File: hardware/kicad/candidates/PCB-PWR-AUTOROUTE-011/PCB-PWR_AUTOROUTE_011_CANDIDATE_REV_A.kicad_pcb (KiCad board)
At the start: 4 copper layers, 90 x 60 mm, 66 parts, among them J1 43045-0213, J2 43045-1202, Q1 CSD18540Q5B, U1 LM74700QDBVRQ1, U2 INA226AIDGSR, U3 LMR604403SRAKR, U4 LMR604403SRAKR, U5 TPS7A2018PDBVR

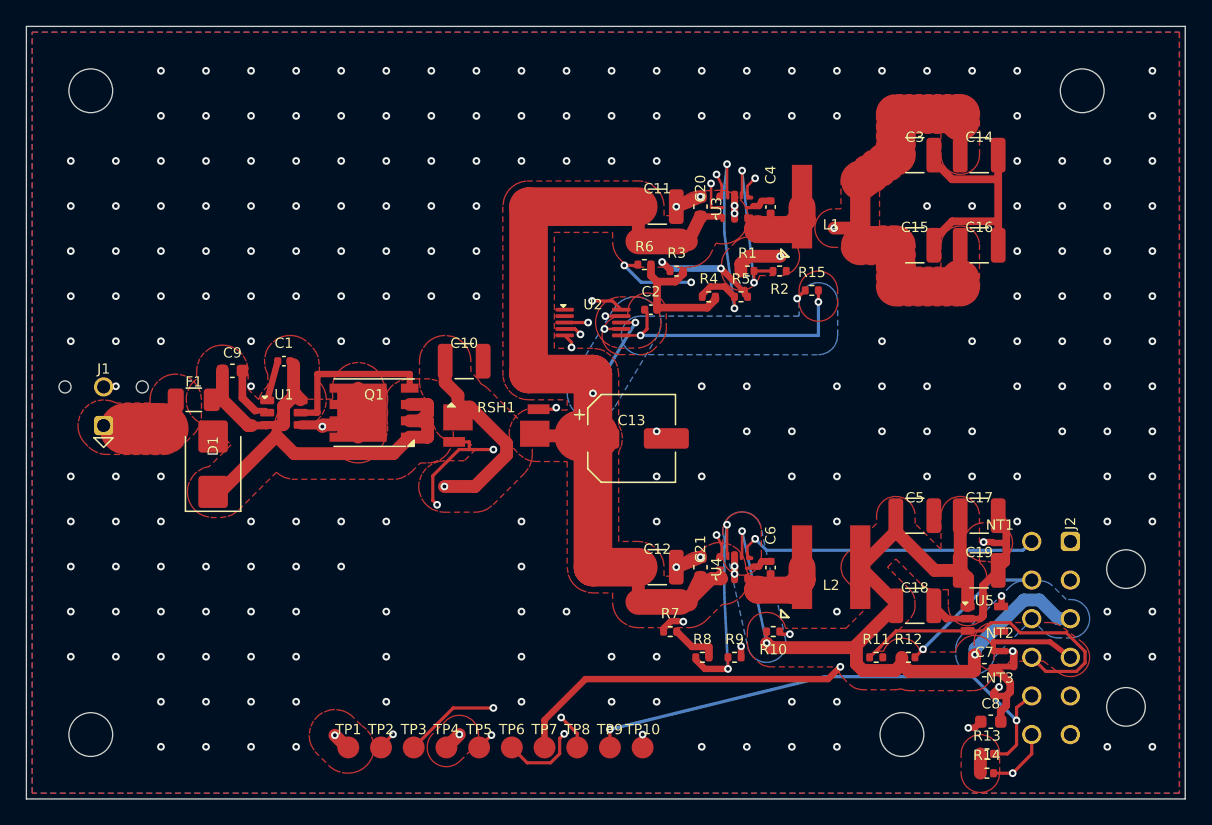
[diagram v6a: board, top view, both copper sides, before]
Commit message: apply: tools/apply_pcb_pwr_autoroute_candidate_rev_a.py
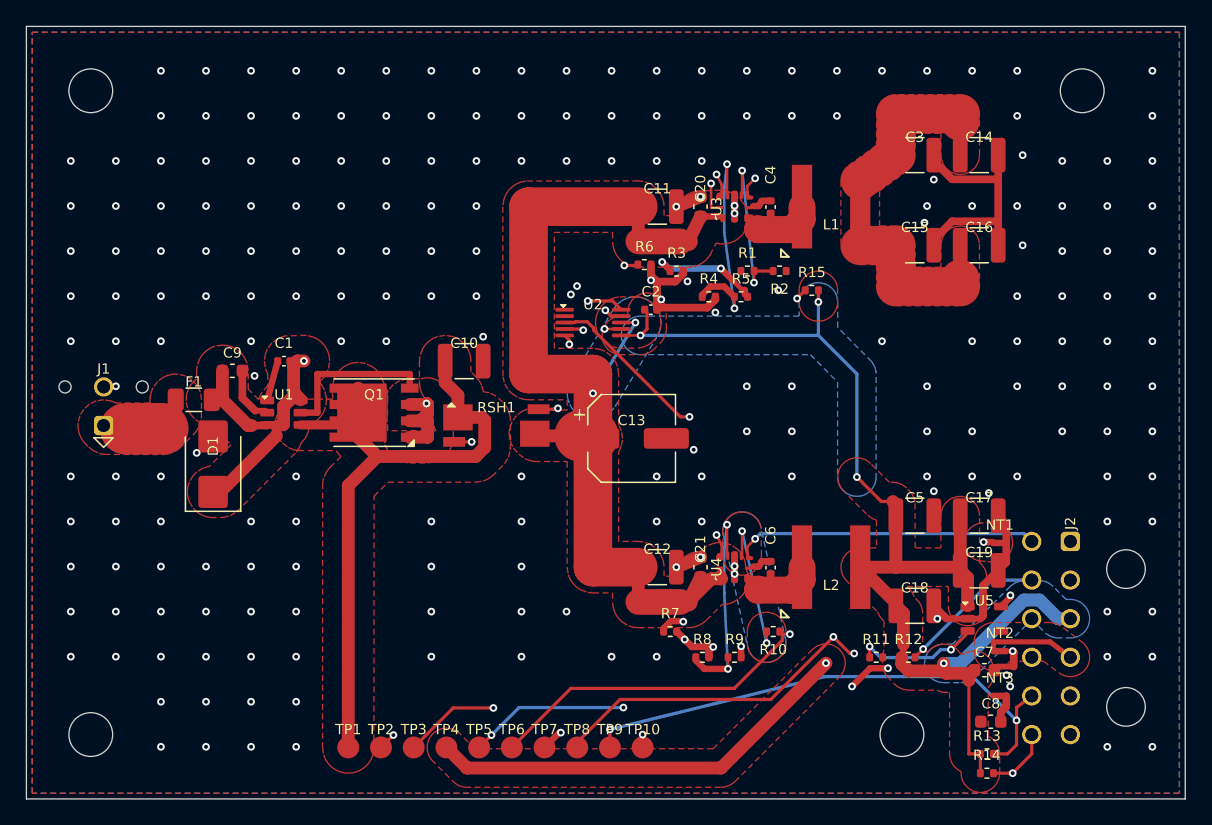
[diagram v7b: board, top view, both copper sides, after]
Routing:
- net 3V8_MODEM: track 144.0 -> 91.7 mm, vias 3 -> 1
- net 1V8_MIC: track 70.4 -> 52.3 mm, vias 3 -> 4
- net 3V3_DIGITAL: track 91.4 -> 106.1 mm, vias 5 -> 6
- net EN_MODEM: track 57.1 -> 67.7 mm, vias 3 -> 2
- net SHUNT_LOAD_SENSE: track 45.3 -> 55.1 mm
- net EN_AUX: track 24.5 -> 16.4 mm, vias 0 -> 2
- net GND_MIC: track 7.95 -> 0.00 mm, vias 1 -> 0
- net VBAT_PROTECTED: track 60.1 -> 52.6 mm, vias 3 -> 0
- net PWR_GOOD: track 65.0 -> 58.0 mm, vias 3 -> 2
- net I2C2_SDA: track 83.1 -> 77.7 mm
- net PG_3V8: track 67.0 -> 63.3 mm, vias 3 -> 4
- net I2C2_SCL: track 78.2 -> 75.0 mm
- net GND_PWR: track 65.5 -> 62.7 mm, vias 220 -> 224
- net SHUNT_SOURCE_SENSE: track 47.8 -> 45.6 mm, vias 4 -> 3
- net FAULT: track 77.0 -> 77.6 mm, vias 3 -> 4
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- added copper zone on In2.Cu, net VBAT_FUSED
- removed copper zone on In2.Cu, net VBAT_PROTECTED

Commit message: apply: tools/apply_pcb_pwr_autoroute_candidate_rev_a.py
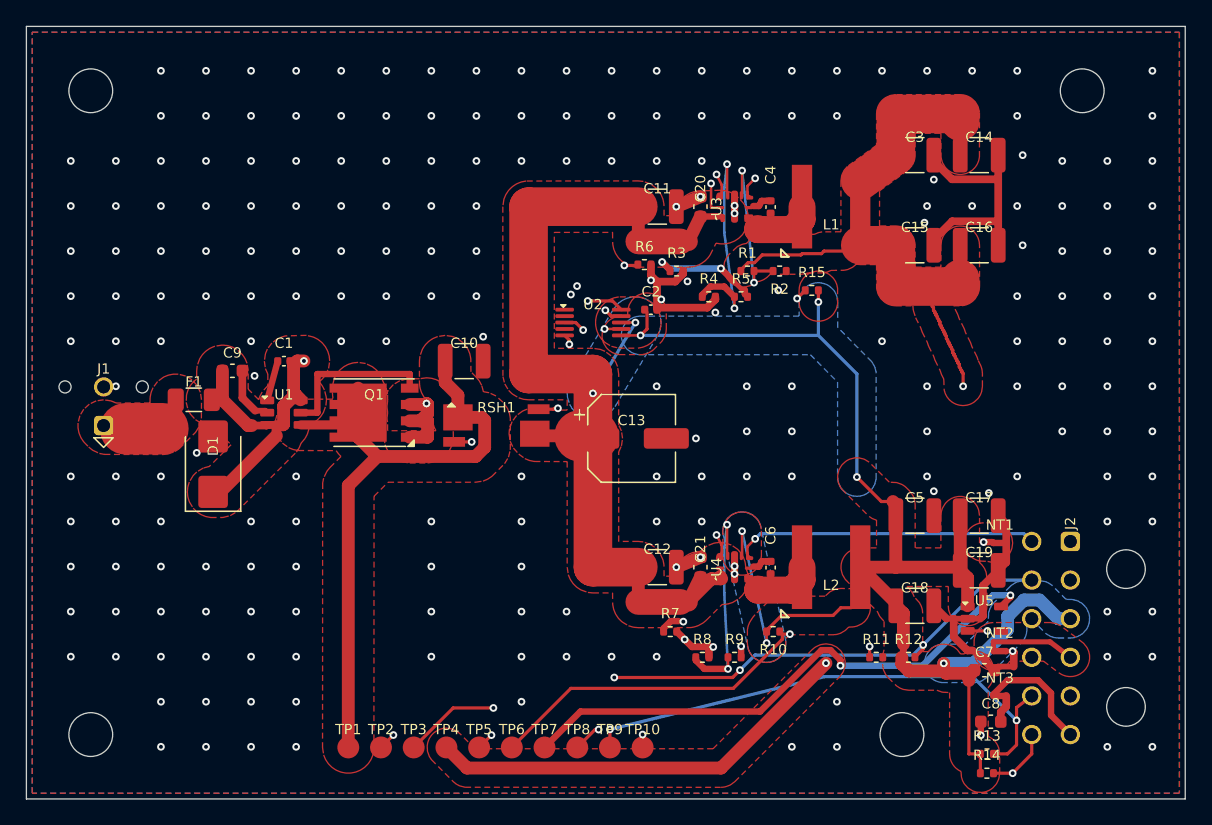
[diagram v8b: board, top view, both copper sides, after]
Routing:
- net I2C2_SDA: track 77.7 -> 40.6 mm, vias 3 -> 2
- net 3V8_MODEM: track 91.7 -> 117.3 mm, vias 1 -> 2
- net 1V8_MIC: track 52.3 -> 68.4 mm, vias 4 -> 3
- net GND_MIC: track 0.00 -> 9.31 mm
- net 3V3_DIGITAL: track 106.1 -> 114.0 mm
- net GND_PWR: track 62.7 -> 68.8 mm, vias 224 -> 225
- net PG_3V8: track 63.3 -> 65.1 mm, vias 4 -> 3
- net FAULT: track 77.6 -> 77.4 mm, vias 4 -> 5
